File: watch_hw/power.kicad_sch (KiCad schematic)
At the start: 14 parts, among them U2 nPM1100-QDAA, U3 MAX17048G+

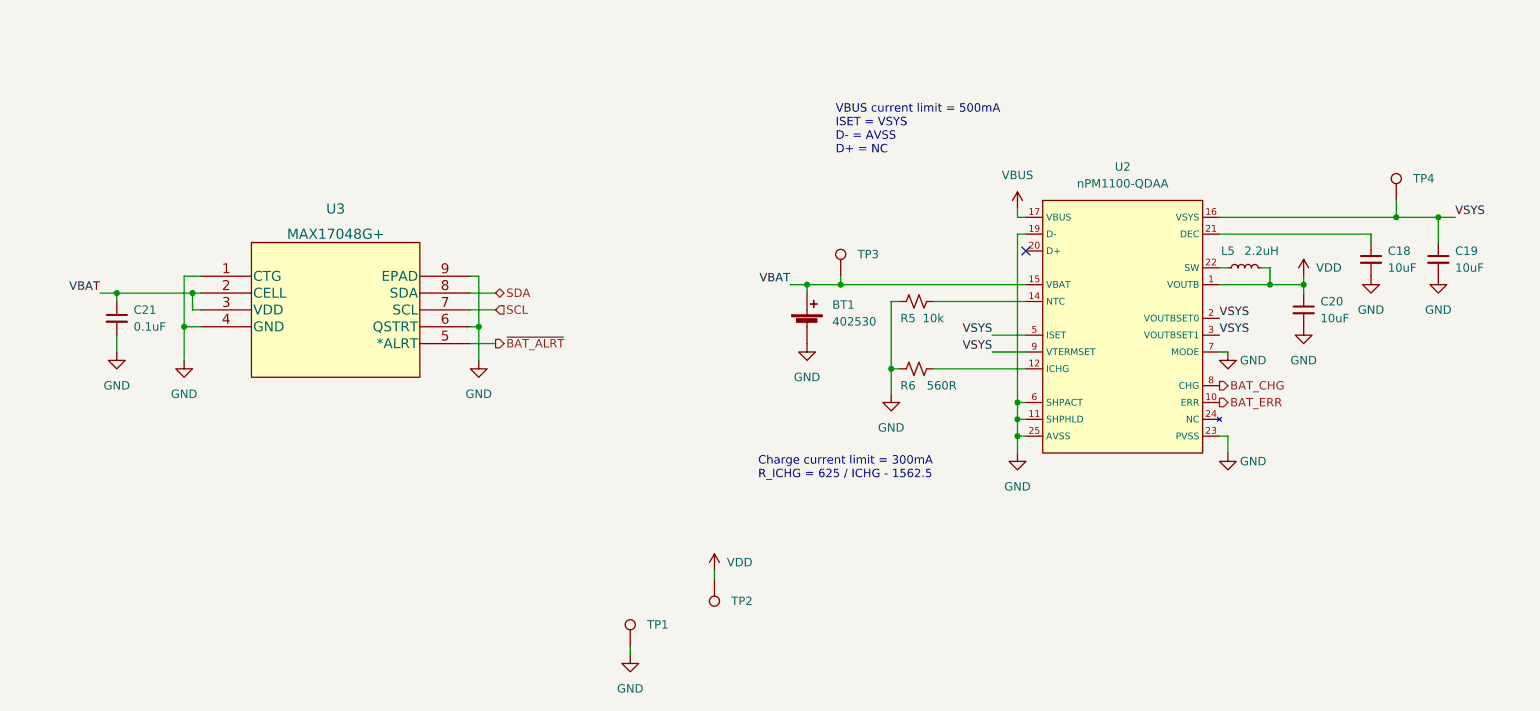
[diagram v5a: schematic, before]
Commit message: Add manufacturer/PN fields, select LCSC parts
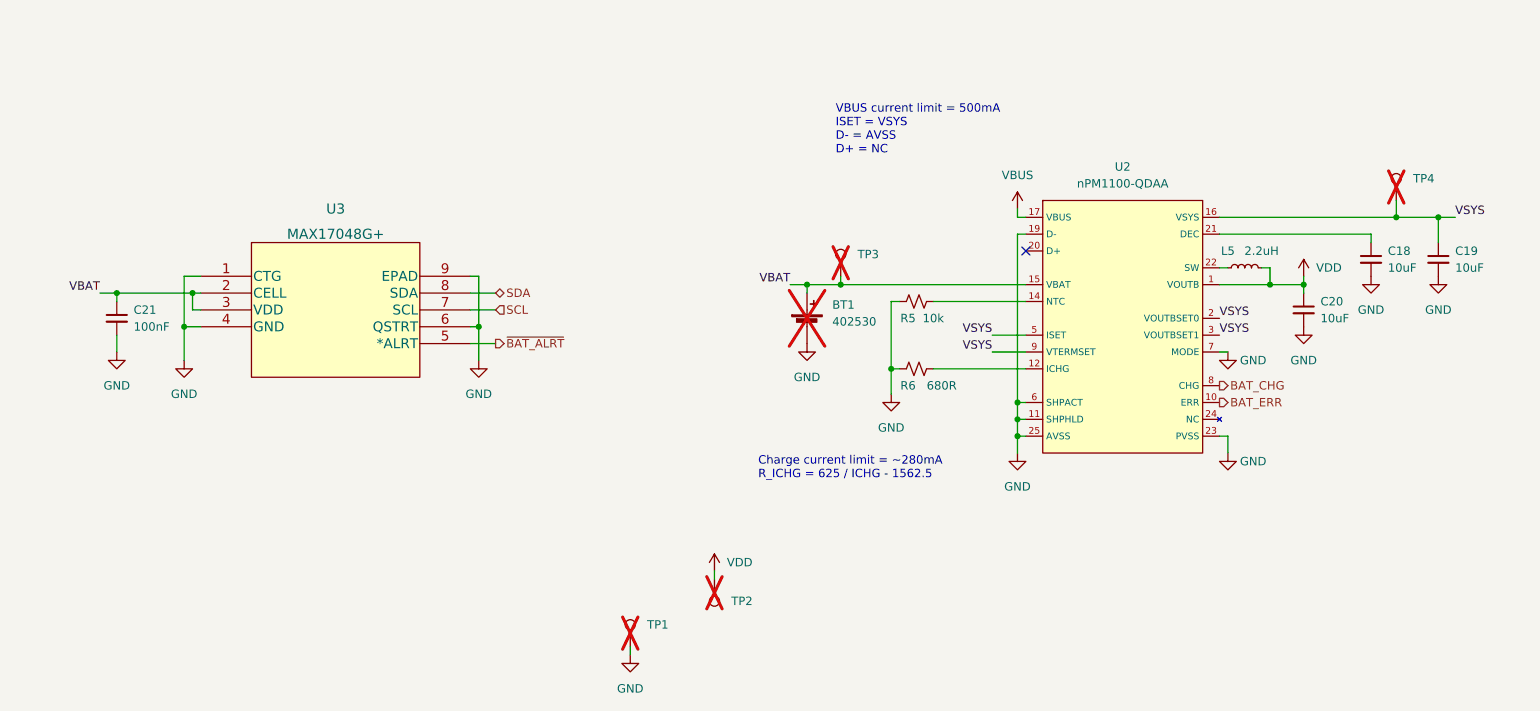
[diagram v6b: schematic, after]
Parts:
- BT1, TP1, TP2, TP3, TP4: now not fitted
- C18, C19, C20: LCSC (none) -> C15850
- C21: value 0.1uF -> 100nF; LCSC (none) -> C1525
- R5: LCSC (none) -> C25744
- R6: value 560R -> 680R; LCSC (none) -> C25130
- U2: LCSC (none) -> C5816773
- U3: LCSC (none) -> C2682616
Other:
- note added: "Charge current limit = ~280mA R_ICHG = 625 / ICHG - 1562.5"
- note removed: "Charge current limit = 300mA R_ICHG = 625 / ICHG - 1562.5"
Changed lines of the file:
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@@
 	(generator_version "9.0")
 	(paper "A4")
-	(text "Charge current limit = 300mA\nR_ICHG = 625 / ICHG - 1562.5"
+	(text "Charge current limit = ~280mA\nR_ICHG = 625 / ICHG - 1562.5"
 		(exclude_from_sim no)
 		(at 146.304 111.506 0)
@@
 		(in_bom yes)
 		(on_board yes)
-		(dnp no)
+		(dnp yes)
 		(fields_autoplaced yes)
 		(property "Reference" "BT1"
@@
 		(in_bom yes)
 		(on_board yes)
-		(dnp no)
+		(dnp yes)
 		(fields_autoplaced yes)
 		(property "Reference" "TP4"
@@
 			)
 		)
+		(property "LCSC" "C5816773"
+			(at 186.69 73.66 0)
+			(effects
+				(font
+					(size 1.27 1.27)
+				)
+				(hide yes)
+			)
+		)
 		(pin "17"
 		)
@@
 		(in_bom yes)
 		(on_board yes)
-		(dnp no)
+		(dnp yes)
 		(fields_autoplaced yes)
 		(property "Reference" "TP1"
@@
 			)
 		)
+		(property "LCSC" "C15850"
+			(at 238.76 80.01 0)
+			(effects
+				(font
+					(size 1.27 1.27)
+				)
+				(hide yes)
+			)
+		)
 		(pin "1"
 		)
@@
 			)
 		)
+		(property "LCSC" "C15850"
+			(at 248.92 80.01 0)
+			(effects
+				(font
+					(size 1.27 1.27)
+				)
+				(hide yes)
+			)
+		)
 		(pin "1"
 		)
@@
 			)
 		)
+		(property "LCSC" "C2682616"
+			(at 62.23 82.55 0)
+			(effects
+				(font
+					(size 1.27 1.27)
+				)
+				(hide yes)
+			)
+		)
 		(pin "1"
 		)
@@
 		(in_bom yes)
 		(on_board yes)
-		(dnp no)
+		(dnp yes)
 		(fields_autoplaced yes)
 		(property "Reference" "TP2"
@@
 			)
 		)
+		(property "LCSC" "C25744"
+			(at 170.18 86.36 90)
+			(effects
+				(font
+					(size 1.27 1.27)
+				)
+				(hide yes)
+			)
+		)
 		(pin "1"
 		)
@@
 			)
 		)
-		(property "Value" "560R"
+		(property "Value" "680R"
 			(at 173.99 99.06 90)
 			(effects
@@
 		(property "Description" ""
 			(at 170.18 96.52 0)
+			(effects
+				(font
+					(size 1.27 1.27)
+				)
+				(hide yes)
+			)
+		)
+		(property "LCSC" "C25130"
+			(at 170.18 96.52 90)
 			(effects
 				(font
@@
 			)
 		)
+		(property "LCSC" "C15850"
+			(at 228.6 87.63 0)
+			(effects
+				(font
+					(size 1.27 1.27)
+				)
+				(hide yes)
+			)
+		)
 		(pin "1"
 		)
@@
 			)
 		)
-		(property "Value" "0.1uF"
+		(property "Value" "100nF"
 			(at 52.07 90.1762 0)
 			(effects
@@
 		)
 		(property "Description" ""
+			(at 49.53 88.9 0)
+			(effects
+				(font
+					(size 1.27 1.27)
+				)
+				(hide yes)
+			)
+		)
+		(property "LCSC" "C1525"
 			(at 49.53 88.9 0)
 			(effects
@@
 		(in_bom yes)
 		(on_board yes)
-		(dnp no)
+		(dnp yes)
 		(fields_autoplaced yes)
 		(property "Reference" "TP3"

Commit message: Finish adding MPN info
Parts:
- C18, C19, C20: Manufacturer (none) -> Samsung; Manufacturer Part Number (none) -> CL21A106KAYNNNE
- C21: Manufacturer (none) -> Samsung; Manufacturer Part Number (none) -> CL05B104KO5NNNC
- L5: LCSC (none) -> C341781; Manufacturer (none) -> Murata; Manufacturer Part Number (none) -> LQM21PN2R2MGHL
- R5: Manufacturer (none) -> UNI-ROYAL; Manufacturer Part Number (none) -> 0402WGF1002TCE
- R6: Manufacturer (none) -> UNI-ROYAL; Manufacturer Part Number (none) -> 0402WGF6800TCE
- U2: Manufacturer Part Number (none) -> NPM1100-QDAA-R
- U3: Manufacturer (none) -> Maxim Integrated; Manufacturer Part Number (none) -> MAX17048G+T10
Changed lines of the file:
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@@
+			)
+		)
+		(property "Manufacturer Part Number" "NPM1100-QDAA-R"
+			(at 186.69 73.66 0)
+			(effects
+				(font
+					(size 1.27 1.27)
+				)
+				(hide yes)
 			)
 		)
@@
 		(property "Description" ""
 			(at 219.71 81.28 0)
+			(effects
+				(font
+					(size 1.27 1.27)
+				)
+				(hide yes)
+			)
+		)
+		(property "LCSC" "C341781"
+			(at 219.71 81.28 90)
+			(effects
+				(font
+					(size 1.27 1.27)
+				)
+				(hide yes)
+			)
+		)
+		(property "Manufacturer" "Murata"
+			(at 219.71 81.28 90)
+			(effects
+				(font
+					(size 1.27 1.27)
+				)
+				(hide yes)
+			)
+		)
+		(property "Manufacturer Part Number" "LQM21PN2R2MGHL"
+			(at 219.71 81.28 90)
 			(effects
 				(font
@@
 			)
 		)
+		(property "Manufacturer" "Samsung"
+			(at 238.76 80.01 0)
+			(effects
+				(font
+					(size 1.27 1.27)
+				)
+				(hide yes)
+			)
+		)
+		(property "Manufacturer Part Number" "CL21A106KAYNNNE"
+			(at 238.76 80.01 0)
+			(effects
+				(font
+					(size 1.27 1.27)
+				)
+				(hide yes)
+			)
+		)
 		(pin "1"
 		)
@@
 			)
 		)
+		(property "Manufacturer" "Samsung"
+			(at 248.92 80.01 0)
+			(effects
+				(font
+					(size 1.27 1.27)
+				)
+				(hide yes)
+			)
+		)
+		(property "Manufacturer Part Number" "CL21A106KAYNNNE"
+			(at 248.92 80.01 0)
+			(effects
+				(font
+					(size 1.27 1.27)
+				)
+				(hide yes)
+			)
+		)
 		(pin "1"
 		)
@@
 			)
 		)
+		(property "Manufacturer" "Maxim Integrated"
+			(at 62.23 82.55 0)
+			(effects
+				(font
+					(size 1.27 1.27)
+				)
+				(hide yes)
+			)
+		)
+		(property "Manufacturer Part Number" "MAX17048G+T10"
+			(at 62.23 82.55 0)
+			(effects
+				(font
+					(size 1.27 1.27)
+				)
+				(hide yes)
+			)
+		)
 		(pin "1"
 		)
@@
 			)
 		)
+		(property "Manufacturer" "UNI-ROYAL"
+			(at 170.18 86.36 90)
+			(effects
+				(font
+					(size 1.27 1.27)
+				)
+				(hide yes)
+			)
+		)
+		(property "Manufacturer Part Number" "0402WGF1002TCE"
+			(at 170.18 86.36 90)
+			(effects
+				(font
+					(size 1.27 1.27)
+				)
+				(hide yes)
+			)
+		)
 		(pin "1"
 		)
@@
 			)
 		)
+		(property "Manufacturer" "UNI-ROYAL"
+			(at 170.18 96.52 90)
+			(effects
+				(font
+					(size 1.27 1.27)
+				)
+				(hide yes)
+			)
+		)
+		(property "Manufacturer Part Number" "0402WGF6800TCE"
+			(at 170.18 96.52 90)
+			(effects
+				(font
+					(size 1.27 1.27)
+				)
+				(hide yes)
+			)
+		)
 		(pin "1"
 		)
@@
 			)
 		)
+		(property "Manufacturer" "Samsung"
+			(at 228.6 87.63 0)
+			(effects
+				(font
+					(size 1.27 1.27)
+				)
+				(hide yes)
+			)
+		)
+		(property "Manufacturer Part Number" "CL21A106KAYNNNE"
+			(at 228.6 87.63 0)
+			(effects
+				(font
+					(size 1.27 1.27)
+				)
+				(hide yes)
+			)
+		)
 		(pin "1"
 		)
@@
 			(at 49.53 88.9 0)
 			(effects
+				(font
+					(size 1.27 1.27)
+				)
+				(hide yes)
+			)
+		)
+		(property "Manufacturer" "Samsung"
+			(at 49.53 88.9 0)
+			(effects
+				(font
+					(size 1.27 1.27)
+				)
+				(hide yes)
+			)
+		)
+		(property "Manufacturer Part Number" "CL05B104KO5NNNC"
+			(at 49.53 88.9 0)
+			(effects
